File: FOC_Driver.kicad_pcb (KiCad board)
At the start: 2 copper layers, 86 x 84.2 mm, 86 parts, among them IC1 131M61, J1 Conn_01x06_Pin, J2 Conn_01x03, J3 Conn_02x17_Odd_Even, J4 DE9_Socket, J5 RJ45, J6 RJ45, J7 Screw_Terminal_01x16, Q1 AOD413A, Q2 BSS138, Q3 BSS138, Q4 MMBT2222A, Q5 BSS138, SW1 SW_Push, SW3 SW_Push, SW4 SW_Push, U1 ST485E, U2 AZ1117-3.3, U3 AM26LS32ACDR, U4 AP2151AW-7, U5 GD25D10CT, U6 STM32H523RCTx, U7 CSTNE8M00G550000R0, U8 4504, U9 TSR1-2450E

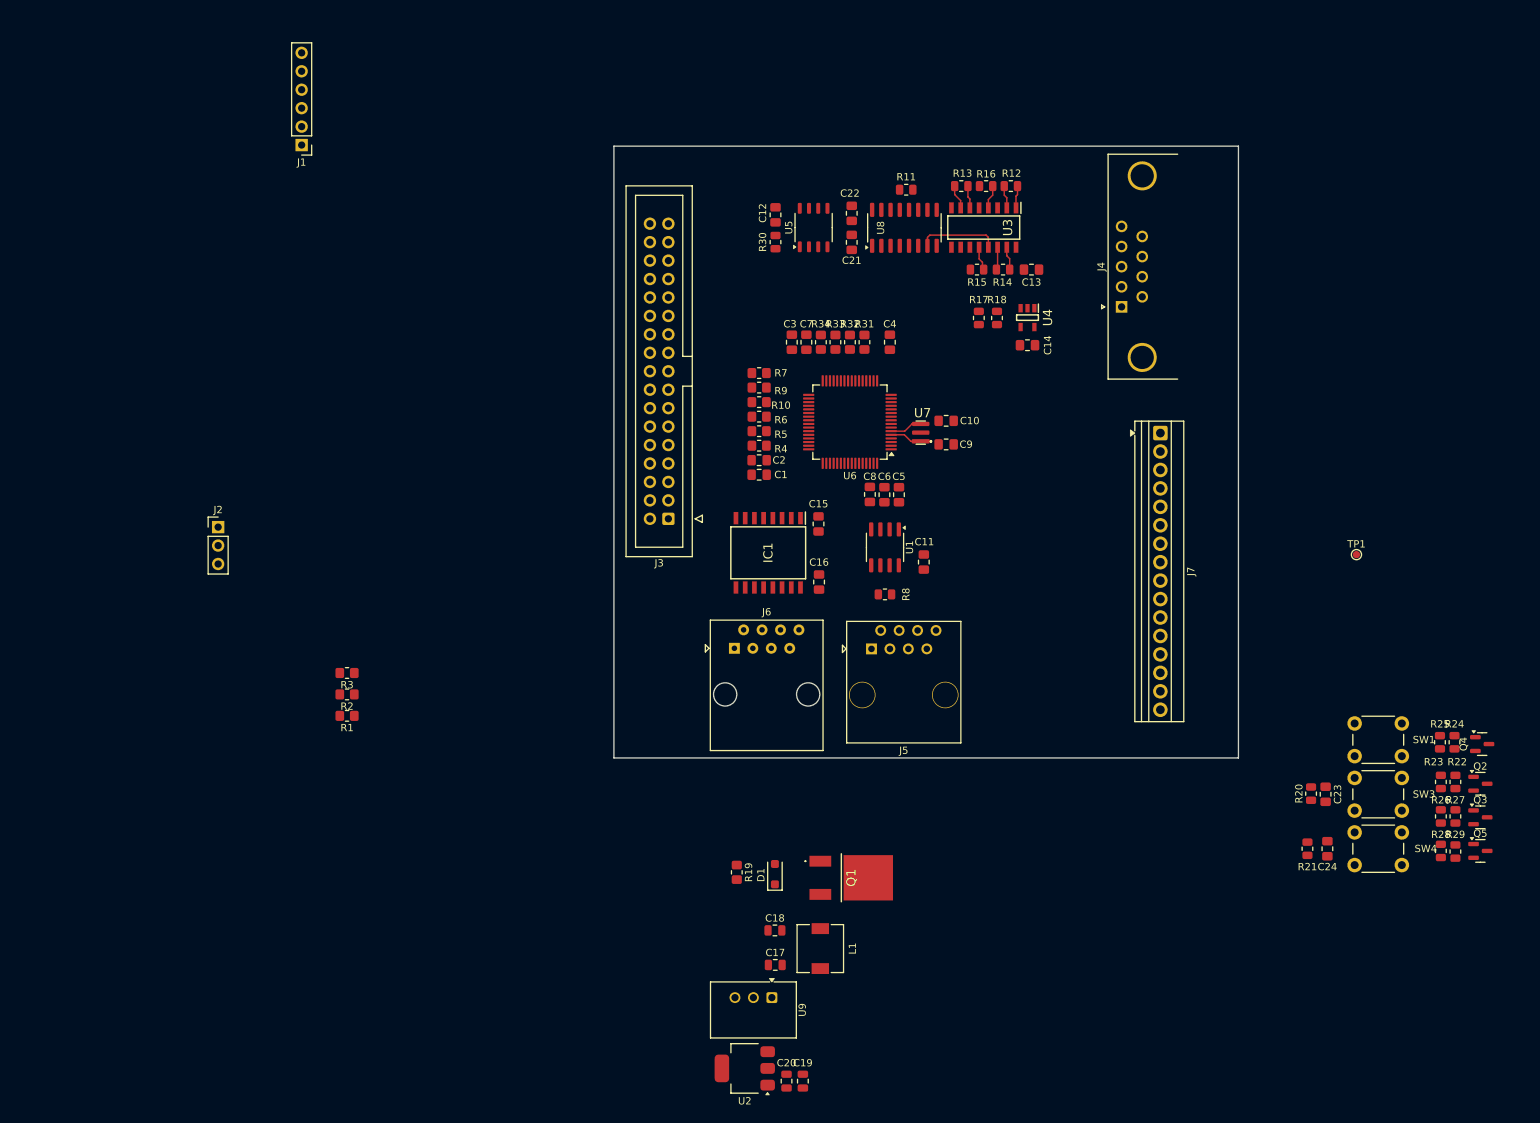
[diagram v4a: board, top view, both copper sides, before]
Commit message: Addition of testpoints
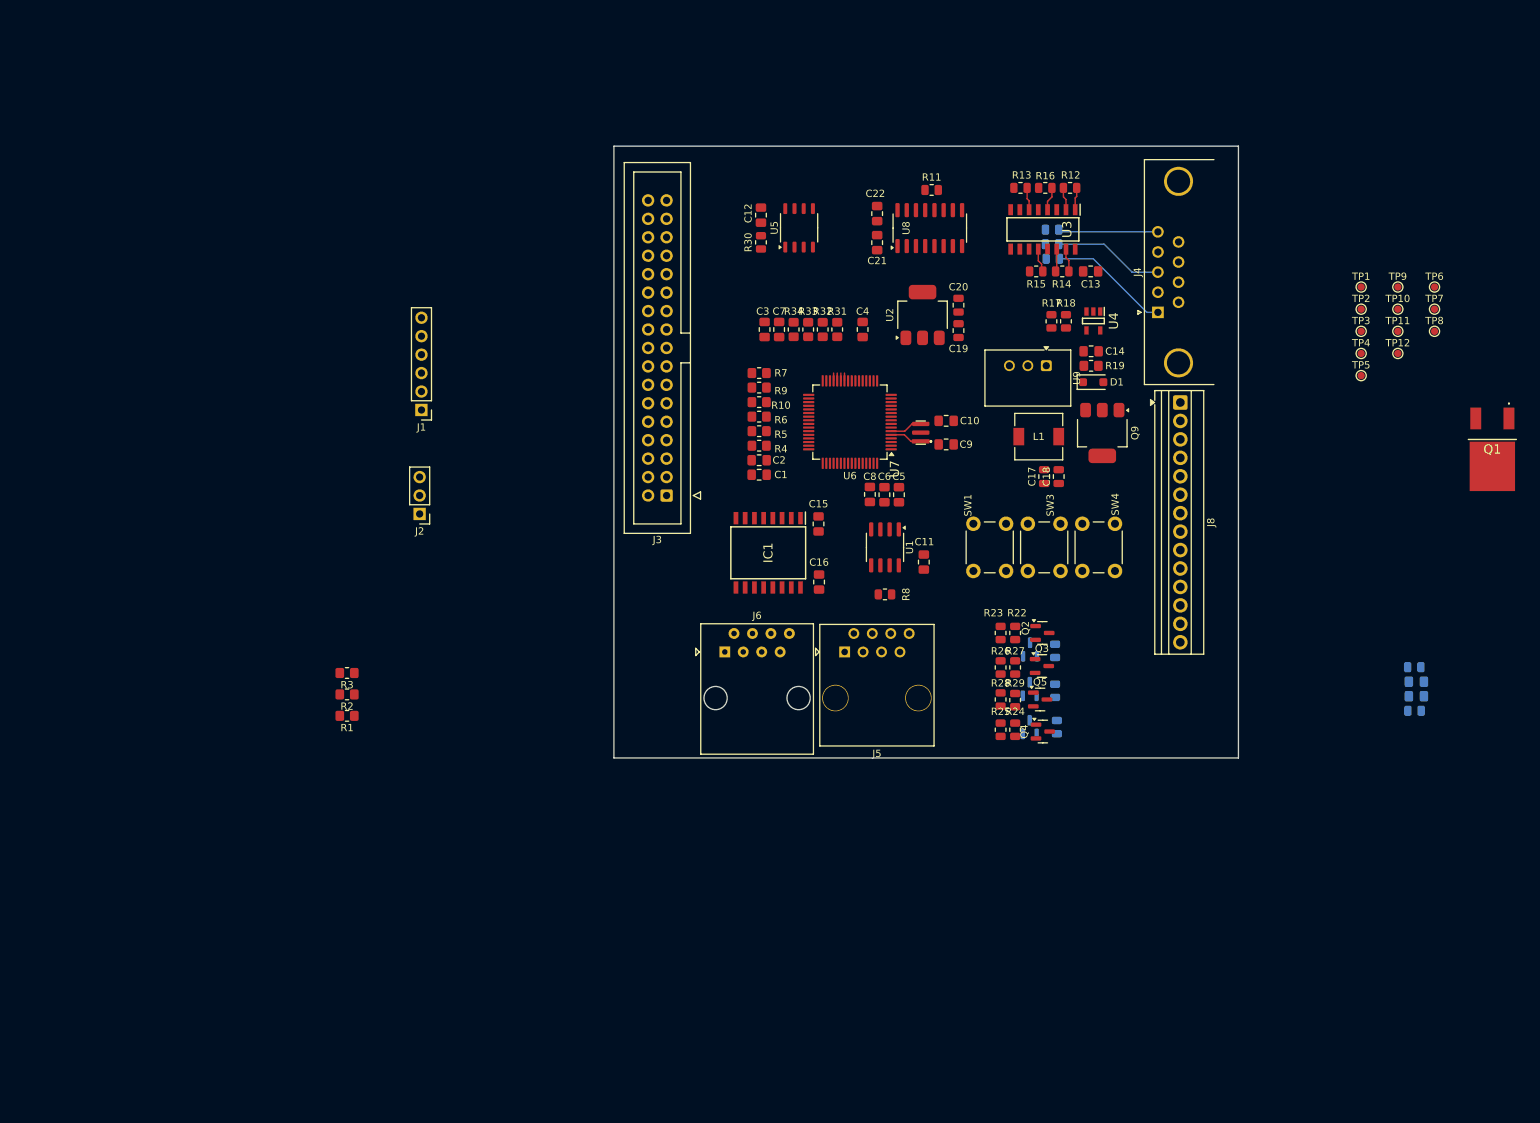
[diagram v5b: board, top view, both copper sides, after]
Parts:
- removed J7: Screw_Terminal_01x16, TerminalBlock:TerminalBlock_Xinya_XY308-2.54-16P_1x16_P2.54mm_Horizontal
- added J8: Screw_Terminal_01x14, TerminalBlock:TerminalBlock_Xinya_XY308-2.54-14P_1x14_P2.54mm_Horizontal, F.Cu at (188.5, 86.3)
- added Q6: MMBT2222A, Package_TO_SOT_SMD:SOT-23, B.Cu at (167.8, 125.8)
- added Q7: MMBT2222A, Package_TO_SOT_SMD:SOT-23, B.Cu at (167.8, 120.3)
- added Q8: MMBT2222A, Package_TO_SOT_SMD:SOT-23, B.Cu at (167.8, 131.0)
- added Q9: ZXMP4A16G, Package_TO_SOT_SMD:SOT-223-3_TabPin2, F.Cu at (177.8, 90.5)
- added R35: 33, Resistor_SMD:R_0805_2012Metric, B.Cu at (171.5, 131.0)
- added R36: 33R, Resistor_SMD:R_0805_2012Metric, B.Cu at (171.2, 120.5)
- added R37: 33R, Resistor_SMD:R_0805_2012Metric, B.Cu at (171.2, 126.0)
- added R38: 0R, Resistor_SMD:R_0805_2012Metric, B.Cu at (170.9, 66.5)
- added R39: 0R, Resistor_SMD:R_0805_2012Metric, B.Cu at (170.8, 64.5)
- added R40: 0R, Resistor_SMD:R_0805_2012Metric, B.Cu at (170.8, 62.5)
- added TP10: SCLK, TestPoint:TestPoint_Pad_D1.0mm, F.Cu at (218.4, 73.5)
- added TP11: MOSI, TestPoint:TestPoint_Pad_D1.0mm, F.Cu at (218.4, 76.5)
- added TP12: nCS, TestPoint:TestPoint_Pad_D1.0mm, F.Cu at (218.4, 79.5)
- added TP2: Encoder_Enable, TestPoint:TestPoint_Pad_D1.0mm, F.Cu at (213.4, 73.5)
- added TP3: Encoder_A, TestPoint:TestPoint_Pad_D1.0mm, F.Cu at (213.4, 76.5)
- added TP4: Encoder_B, TestPoint:TestPoint_Pad_D1.0mm, F.Cu at (213.4, 79.5)
- added TP5: Encoder_C, TestPoint:TestPoint_Pad_D1.0mm, F.Cu at (213.4, 82.6)
- added TP6: RS485_Tx, TestPoint:TestPoint_Pad_D1.0mm, F.Cu at (223.5, 70.4)
- added TP7: RS485_DE, TestPoint:TestPoint_Pad_D1.0mm, F.Cu at (223.5, 73.5)
- added TP8: RS485_Rx, TestPoint:TestPoint_Pad_D1.0mm, F.Cu at (223.5, 76.5)
- added TP9: MISO, TestPoint:TestPoint_Pad_D1.0mm, F.Cu at (218.4, 70.4)
- C23, C24, R20, R21: moved to B.Cu
- R22: value 100k -> 33R
- TP1: value TestPoint -> Encoder_Flag
- moved C20 109.4 mm to (157.9, 72.9)
- moved U2 106.6 mm to (153.0, 74.2), turned to 90 degrees
- moved Q1 105.9 mm to (231.5, 93.0), turned to 180 degrees
- moved C19 105.5 mm to (157.9, 76.4), turned to -90 degrees
- moved U9 94.9 mm to (170.0, 81.2)
- moved R19 85.1 mm to (176.2, 81.2), turned to 0 degrees
- moved D1 80.7 mm to (176.5, 83.5), turned to 0 degrees
- moved C17 76.8 mm to (169.8, 96.5), turned to 90 degrees
- moved L1 76.6 mm to (169.0, 91.0), turned to 180 degrees
- moved C18 73.7 mm to (171.8, 96.5), turned to 90 degrees
- moved Q5 64.1 mm to (169.2, 127.2)
- moved R28 64.1 mm to (163.8, 127.2)
- moved R29 64.1 mm to (165.8, 127.3)
- moved R22 64.0 mm to (165.8, 118.0)
- moved R23 64.0 mm to (163.8, 118.0)
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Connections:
- Q1 pad 1: Net-(D1-A) -> unconnected-(Q1-G-Pad1)
- Q1 pad 2: +24V -> unconnected-(Q1-D-Pad2)
- Q1 pad 3: Net-(D1-K) -> unconnected-(Q1-S-Pad3)
- Q2 pad 2: GNDD -> Net-(Q2-S)
- Q3 pad 2: GNDD -> Net-(Q3-S)
- Q5 pad 2: GNDD -> Net-(Q5-S)
- R15 pad 1: GNDD -> Net-(R15-Pad1)
- R16 pad 1: /Encoder/5V_Encoder -> Net-(R15-Pad1)
- R18 pad 2: /Encoder/Encoder_En -> /Encoder/Encoder_Pwr_En
- TP1 pad 1: unconnected-(TP1-Pad1) -> /Encoder/Encoder_Flg
- U6 pad 10: unconnected-(U6-PC2-Pad10) -> /Encoder/Encoder_En
- U6 pad 13: unconnected-(U6-VDDA-Pad13) -> +3.3V
- U6 pad 33: unconnected-(U6-PB12-Pad33) -> /MCU/ESTOP
- U6 pad 37: unconnected-(U6-PC6-Pad37) -> /Connectors/SoftwareBrake
- U6 pad 38: unconnected-(U6-PC7-Pad38) -> /Connectors/BypassRelay
- U6 pad 50: unconnected-(U6-PA15(JTDI)-Pad50) -> /MCU/RS485_DE
- U6 pad 51: unconnected-(U6-PC10-Pad51) -> /MCU/RS485_Tx
- U6 pad 52: unconnected-(U6-PC11-Pad52) -> /MCU/RS485_Rx
- U6 pad 8: unconnected-(U6-PC0-Pad8) -> /Encoder/Encoder_Pwr_En
- U6 pad 9: unconnected-(U6-PC1-Pad9) -> /Encoder/Encoder_Flg
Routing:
- net /Encoder/A: track 3.08 -> 19.7 mm
- net /Encoder/B: track 3.11 -> 18.4 mm
- net /Encoder/0: track 3.14 -> 16.9 mm
- net Net-(U3-4Y): track 11.2 -> 0.00 mm
- net /Encoder//B: track 3.34 -> 0.00 mm
- net /MCU/SCLK: track 0.00 -> 1.08 mm
- net /MCU/nCS: track 0.00 -> 1.08 mm
- net /MCU/MOSI: track 0.00 -> 1.08 mm
- net /MCU/MISO: track 0.00 -> 1.08 mm
